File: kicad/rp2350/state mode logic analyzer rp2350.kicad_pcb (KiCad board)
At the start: 4 copper layers, 65.9 x 81.5 mm, 154 parts, among them J1 USB0, J2 5V USB0, J3 Probe_Hi, J4 Probe Power, J5 Probe_Lo, J6 Probe Power, J7 SWD0, SW1 Reset 0, SW2 Boot 0, U12 SN74LVC8T245, U13 SN74LVC2T45DCUR, U2 RP2350_80QFN, U4 SN74LVC8T245, U5 SN74LVC8T245, U6 SN74LVC8T245, U7 IS25LP128F-JBLE, U9 MCP1826S, Y1 ECS-120-18-33-JEM-TR

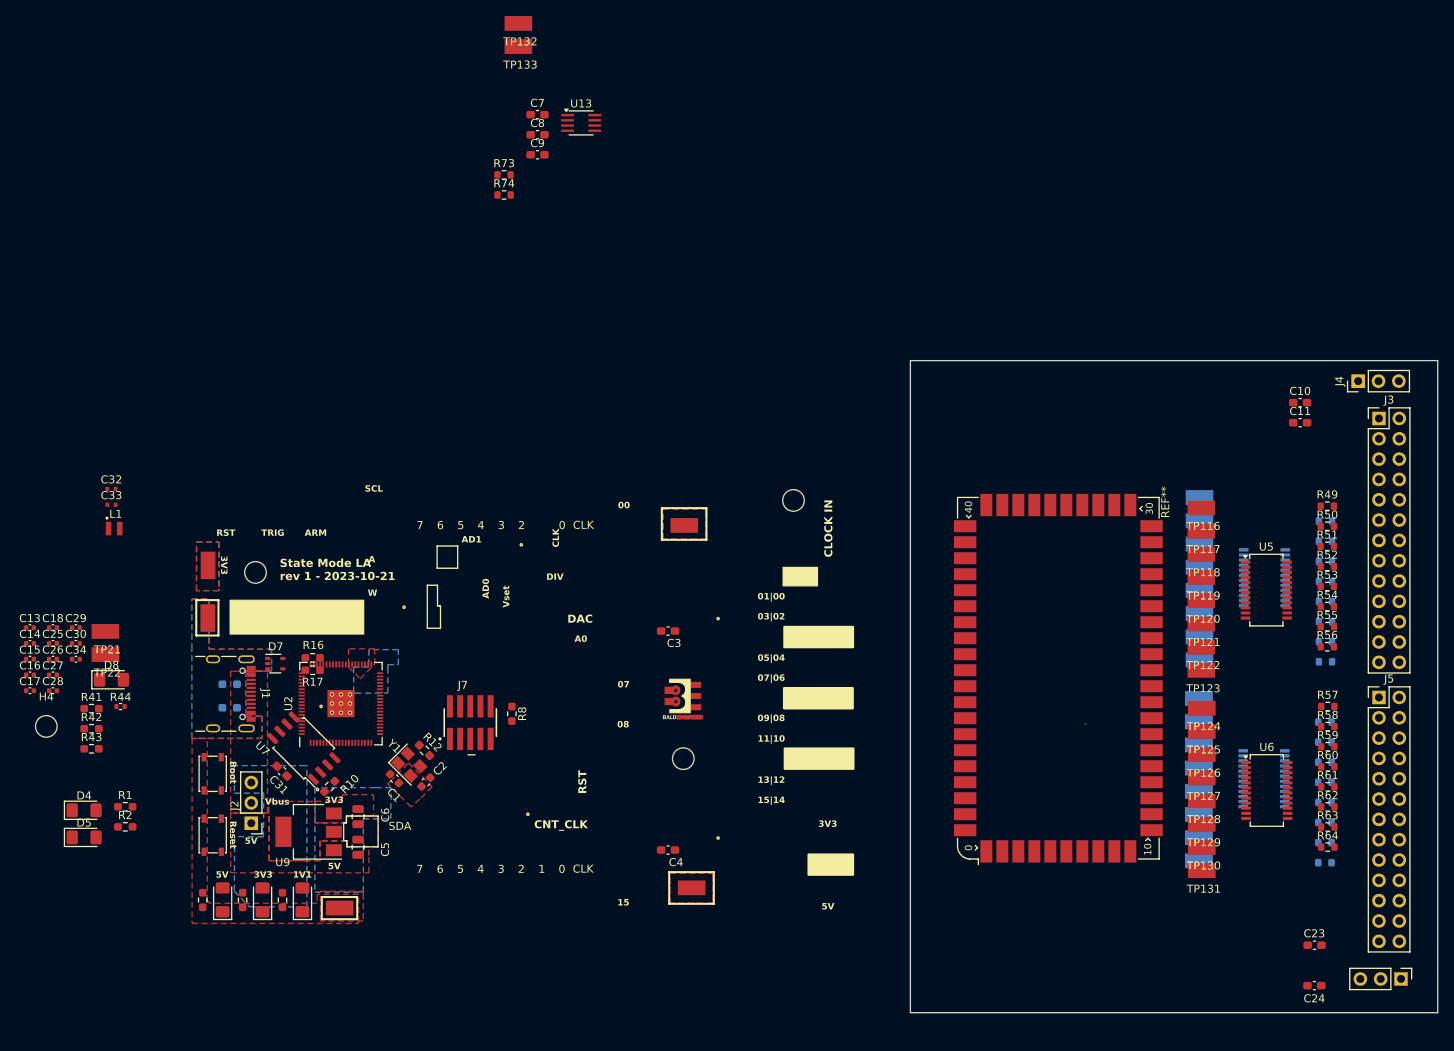
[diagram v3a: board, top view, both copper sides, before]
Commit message: early pcb layout - need to build a demo/test board next
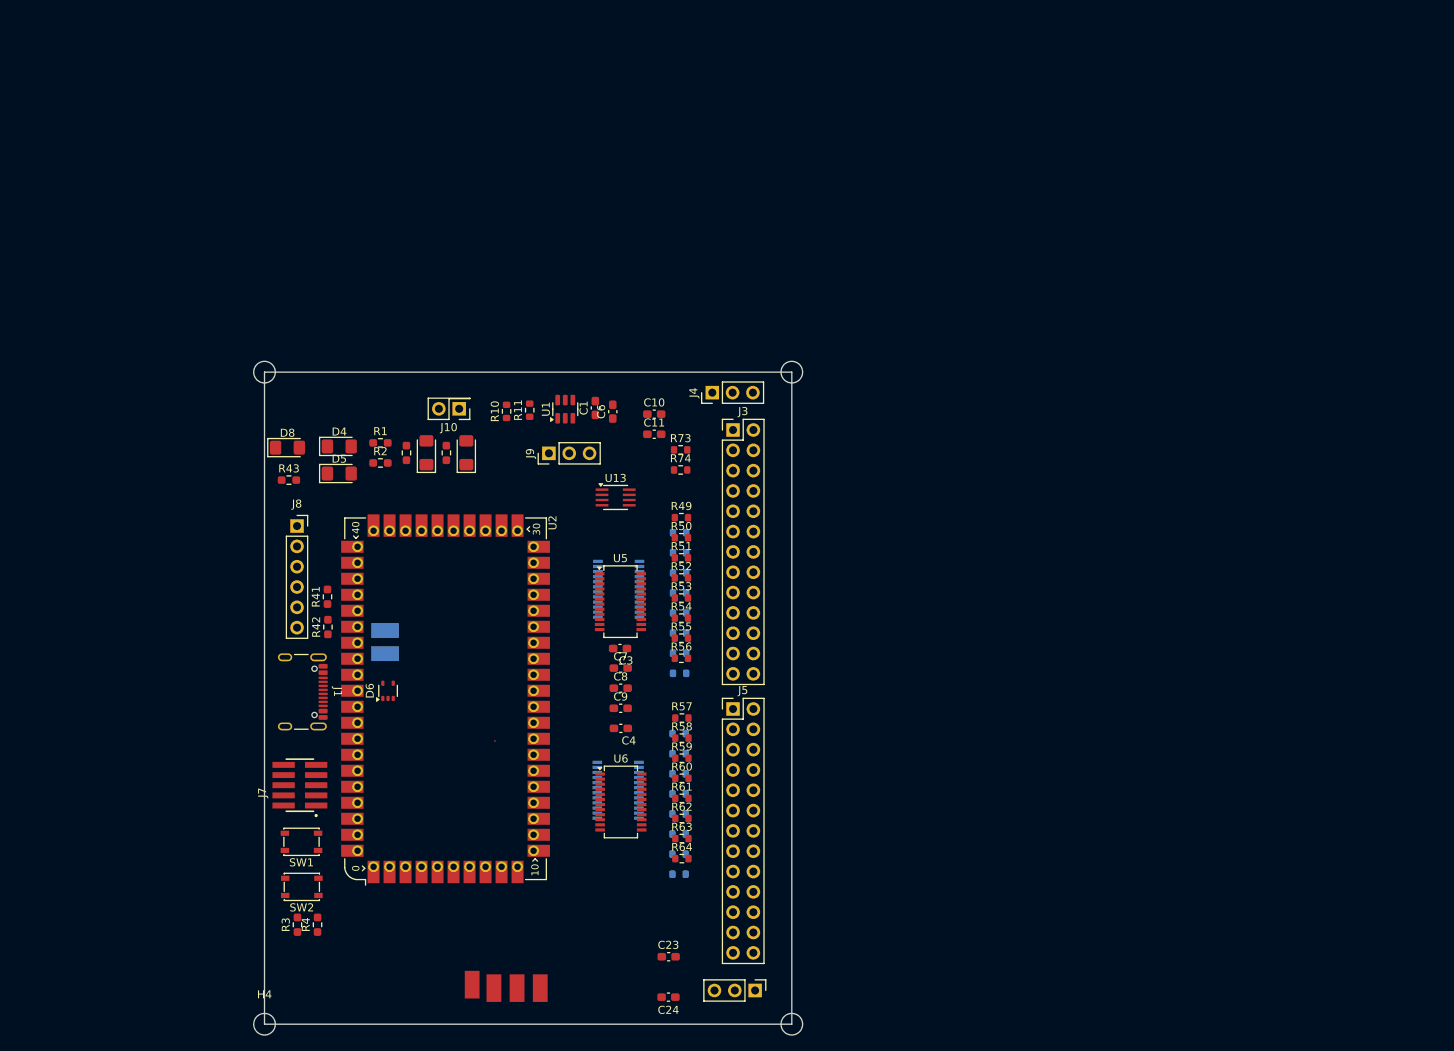
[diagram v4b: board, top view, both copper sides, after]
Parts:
- removed C13, C15, C16, C17, C18, C25, C26, C27, C28, C29, C30: 100n, Capacitor_SMD:C_0402_1005Metric
- removed C14, C34: 4.7u, Capacitor_SMD:C_0402_1005Metric
- removed C2: 27p, Capacitor_SMD:C_0603_1608Metric
- removed C31: 1u, Capacitor_SMD:C_0603_1608Metric_Pad1.08x0.95mm_HandSolder
- removed C32, C33: 4.7u, RP2350_80QFN_minimal:C_0402_1005Metric_small_pads
- removed C5: 10u, Capacitor_SMD:C_0805_2012Metric
- removed D3: 1v1, LED_SMD:LED_1206_3216Metric_Pad1.42x1.75mm_HandSolder
- removed D7: BZA856AVL, Package_TO_SOT_SMD:SOT-353_SC-70-5
- removed J2: 5V USB0, Connector_PinHeader_2.54mm:PinHeader_1x03_P2.54mm_Vertical
- removed L1: 3.3u, RP2350_80QFN_minimal:L_pol_2016
- removed R12: 0, Resistor_SMD:R_0603_1608Metric_Pad0.98x0.95mm_HandSolder
- removed R16, R17: 27, Resistor_SMD:R_0603_1608Metric_Pad0.98x0.95mm_HandSolder
- removed R23, R24: 5k1, Resistor_SMD:R_0603_1608Metric_Pad0.98x0.95mm_HandSolder
- removed R44: 33, Resistor_SMD:R_0402_1005Metric
- removed R7, R8: 4k7, Resistor_SMD:R_0603_1608Metric_Pad0.98x0.95mm_HandSolder
- removed REF**: RP2xxx_Stamp_XL_SMD, KiCad:RP2xxx_Stamp_XL_SMD
- removed REF**: KiCad-Logo_5mm_SilkScreen, Symbol:KiCad-Logo_5mm_SilkScreen
- removed REF**: OSHW-Symbol_8.9x8mm_SilkScreen, Symbol:OSHW-Symbol_8.9x8mm_SilkScreen
- removed TP100, TP101, TP102, TP103, TP104, TP105, TP106, TP107, TP108, TP109, TP110, TP111, TP112, TP113, TP114, TP115, TP116, TP117, TP118, TP119, TP120, TP121, TP122, TP123, TP124, TP125, TP126, TP127, TP128, TP129, TP130, TP131, TP132, TP133, TP15: TestPoint_Harwin, My Libraries:Harwin-S1751-46-Test-Point
- removed U7: IS25LP128F-JBLE, Package_SO:SOIC-8_5.23x5.23mm_P1.27mm
- removed U9: MCP1826S, Package_TO_SOT_SMD:SOT-223
- removed Y1: ECS-120-18-33-JEM-TR, Crystal:Crystal_SMD_3225-4Pin_3.2x2.5mm
- removed svg2mod: G***, My Libraries:BE5v2
- added D6: BZA856AVL, Package_TO_SOT_SMD:SOT-353_SC-70-5, F.Cu at (88.1, 57.8)
- added J10: Vcca_select, Connector_PinHeader_2.54mm:PinHeader_2x01_P2.54mm_Vertical, F.Cu at (97.0, 22.5)
- added J8: FTDI Header, Connector_PinSocket_2.54mm:PinSocket_1x06_P2.54mm_Vertical, F.Cu at (76.7, 37.2)
- added J9: Vccb_select, Connector_PinHeader_2.54mm:PinHeader_1x03_P2.54mm_Vertical, F.Cu at (108.2, 28.1)
- added R11: 1k, Resistor_SMD:R_0603_1608Metric, F.Cu at (105.8, 22.7)
- added R3: 5k1, Resistor_SMD:R_0603_1608Metric_Pad0.98x0.95mm_HandSolder, F.Cu at (76.7, 87.0)
- added R4: 5k1, Resistor_SMD:R_0603_1608Metric_Pad0.98x0.95mm_HandSolder, F.Cu at (79.3, 87.0)
- added U1: MCP4725A2T-E/CH, Package_TO_SOT_SMD:SOT-23-6, F.Cu at (110.2, 22.6)
- C1: value 27p -> 100n; footprint Capacitor_SMD:C_0603_1608Metric -> Capacitor_SMD:C_0603_1608Metric_Pad1.08x0.95mm_HandSolder
- C6: footprint Capacitor_SMD:C_0805_2012Metric -> Capacitor_SMD:C_0603_1608Metric_Pad1.08x0.95mm_HandSolder
- D8: value 2040_L0 -> 2350_LED
- R10: value 1k -> 0; footprint Resistor_SMD:R_0603_1608Metric_Pad0.98x0.95mm_HandSolder -> Resistor_SMD:R_0603_1608Metric
- SW1: value Reset 0 -> Reset
- SW2: value Boot 0 -> Boot
- TP21, TP22: moved to B.Cu
- U2: value RP2350_80QFN -> RP2350_Stamp_XL; footprint RP2350_80QFN_minimal:RP2350-QFN-80-1EP_10x10_P0.4mm_EP3.4x3.4mm_ThermalVias -> RP2xxx_Stamp:RP2xxx_Stamp_XL_THT
- moved C24 80.8 mm to (123.1, 96.1)
- moved U12 80.8 mm to (116.8, 70.2)
- moved U4 80.8 mm to (116.9, 45.1)
- moved U5 80.8 mm to (117.1, 46.6)
- moved C10 80.8 mm to (121.3, 23.2)
- moved C11 80.8 mm to (121.3, 25.7)
- moved J3 80.8 mm to (131.2, 25.2)
- moved J4 80.8 mm to (128.6, 20.5)
- moved J5 80.8 mm to (131.2, 60.0)
- moved J6 80.8 mm to (134.0, 95.2)
- moved R57 80.8 mm to (124.8, 61.2)
- moved R58 80.8 mm to (124.8, 63.7)
- moved R59 80.8 mm to (124.8, 66.2)
- moved R60 80.8 mm to (124.8, 68.7)
- moved R61 80.8 mm to (124.8, 71.2)
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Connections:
- C1 pad 1: Net-(U2-XIN) -> Net-(J9-Pin_3)
- C6 pad 1: +3V3 -> +5V
- J1 pad A4: /VBUS -> +5V
- J1 pad A6: /USB_DP -> /DP
- J1 pad A7: /USB_DN -> /DN
- J1 pad A9: /VBUS -> +5V
- J1 pad B4: /VBUS -> +5V
- J1 pad B6: /USB_DP -> /DP
- J1 pad B7: /USB_DN -> /DN
- J1 pad B9: /VBUS -> +5V
- J7 pad 10: /Run -> /Reset
- R1 pad 1: Net-(U2-GPIO47_ADC7) -> /Armed
- R10 pad 1: /~{CS} -> Net-(U1-VOUT)
- R10 pad 2: Net-(R10-Pad2) -> Net-(J9-Pin_3)
- R2 pad 1: Net-(U2-GPIO46_ADC6) -> /Triggered
- R41 pad 2: /SDA -> /I2C1_SDA
- R42 pad 2: /SCL -> /I2C1_SCL
- R43 pad 1: /CNT_RESET -> /2350_LED
- SW1 pad 1: /Run -> /Reset
- SW2 pad 1: Net-(R10-Pad2) -> Net-(U2A-BOOTSEL)
- TP21 pad 1: /SDA -> /I2C1_SDA
- TP22 pad 1: /SCL -> /I2C1_SCL
- U12 pad 1: +3V3 -> Vcca
- U12 pad 2: unconnected-(U12-DIR-Pad2) -> GND
- U12 pad 22: unconnected-(U12-~{OE}-Pad22) -> GND
- U12 pad 23: +3V3 -> Vccb
- U12 pad 24: +3V3 -> Vccb
- U13 pad 1: +3V3 -> Vcca
- U13 pad 5: unconnected-(U13-DIR-Pad5) -> GND
- U13 pad 8: +3V3 -> Vccb
- U2 pad 1: /BUF29 -> /QUAL
- U2 pad 10: +1V1 -> /BUF24
- U2 pad 11: /BUF21 -> /BUF23
- U2 pad 12: /BUF20 -> /BUF22
- U2 pad 13: /BUF19 -> /BUF21
- U2 pad 14: /BUF18 -> /BUF20
- U2 pad 15: +3V3 -> /BUF19
- U2 pad 16: /BUF17 -> /BUF18
- U2 pad 17: /BUF16 -> /BUF17
- U2 pad 18: /QUAL -> /BUF16
- U2 pad 19: /CLK -> /QUAL
- U2 pad 2: /BUF28 -> /CLK
- U2 pad 20: /BUF15 -> /CLK
- U2 pad 21: /BUF14 -> /BUF15
- U2 pad 22: /BUF13 -> /BUF14
- U2 pad 23: /BUF12 -> /BUF13
- U2 pad 24: +3V3 -> /BUF12
- U2 pad 29: +3V3 -> /BUF07
- U2 pad 3: /BUF27 -> /BUF31
- U2 pad 30: Net-(U2-XIN) -> /BUF06
- U2 pad 31: Net-(U2-XOUT) -> GND
- U2 pad 32: +1V1 -> unconnected-(U2A-VBAT-Pad32)_1
- U2 pad 33: /SWCLK -> +5V
- U2 pad 34: /SWD -> +3V3
- U2 pad 35: /Run -> /DN
- U2 pad 36: /BUF07 -> /DP
- U2 pad 37: /BUF06 -> /SWD
- U2 pad 38: /BUF05 -> /SWCLK
- U2 pad 39: /BUF04 -> /Reset
- U2 pad 4: /BUF26 -> /BUF30
- U2 pad 40: /BUF03 -> Net-(U2A-BOOTSEL)
- U2 pad 41: +3V3 -> /BUF05
- U2 pad 42: /BUF02 -> /BUF04
- U2 pad 43: /BUF01 -> /BUF03
- U2 pad 44: /BUF00 -> /BUF02
- U2 pad 45: unconnected-(U2-GPIO36-Pad45) -> /BUF01
- U2 pad 46: unconnected-(U2-GPIO37-Pad46) -> /BUF00
- U2 pad 5: +3V3 -> /BUF29
- U2 pad 50: +3V3 -> unconnected-(U2B-GPIO39-Pad50)
- U2 pad 51: +1V1 -> /Armed
- U2 pad 52: /SDA -> /Triggered
- U2 pad 53: /SCL -> /2350_LED
- U2 pad 54: /CNT_CLK -> unconnected-(U2B-GPIO43-Pad54)_1
- U2 pad 55: /CNT_RESET -> /UART_TX
- U2 pad 56: /LA_Enable -> /UART_RX
- U2 pad 57: Net-(U2-GPIO46_ADC6) -> /I2C1_SDA
- U2 pad 58: Net-(U2-GPIO47_ADC7) -> /I2C1_SCL
- U2 pad 59: +3V3 -> unconnected-(U2A-BAT_STAT-Pad59)
- U2 pad 6: /BUF25 -> /BUF28
- U2 pad 60: +3V3 -> unconnected-(U2A-LDO_EN-Pad60)
- U2 pad 7: /BUF24 -> /BUF27
- U2 pad 8: /BUF23 -> /BUF26
- U2 pad 9: /BUF22 -> /BUF25
- U4 pad 1: +3V3 -> Vcca
- U4 pad 2: unconnected-(U4-DIR-Pad2) -> GND
- U4 pad 22: unconnected-(U4-~{OE}-Pad22) -> GND
- U4 pad 23: +3V3 -> Vccb
- U4 pad 24: +3V3 -> Vccb
- U5 pad 1: +3V3 -> Vcca
- U5 pad 2: unconnected-(U5-DIR-Pad2) -> GND
- U5 pad 22: unconnected-(U5-~{OE}-Pad22) -> GND
- U5 pad 23: +3V3 -> Vccb
- U5 pad 24: +3V3 -> Vccb
- U6 pad 1: +3V3 -> Vcca
- U6 pad 2: unconnected-(U6-DIR-Pad2) -> GND
- U6 pad 22: unconnected-(U6-~{OE}-Pad22) -> GND
- U6 pad 23: +3V3 -> Vccb
- U6 pad 24: +3V3 -> Vccb
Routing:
- removed copper zone on B.Cu, net +3V3
- removed copper zone on F.Cu, net +3V3
- removed copper zone on In2.Cu, net +3V3
- removed copper zone on F.Cu, net +5V
- removed copper zone on F.Cu, net /VBUS
- removed copper zone on B.Cu, net GND
- removed copper zone on F.Cu, net GND
- removed copper zone on In1.Cu, net GND
- removed copper zone on In2.Cu, net GND
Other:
- board text added: "Verify courtyard of FISH"
- board text removed: "0"
- board text removed: "00"
- board text removed: "01|00"
- board text removed: "03|02"
- board text removed: "05|04"
- board text removed: "07"
- board text removed: "07|06"
- board text removed: "08"
- board text removed: "09|08"
- board text removed: "1"
- board text removed: "11|10"
- board text removed: "13|12"
- board text removed: "15"
- board text removed: "15|14"
- board text removed: "1V1"
- board text removed: "2"
- board text removed: "3"
- board text removed: "3V3"
- board text removed: "4"
- board text removed: "5"
- board text removed: "5V"
- board text removed: "6"
- board text removed: "7"
- board text removed: "A"
- board text removed: "A0"
- board text removed: "AD0"
- board text removed: "AD1"
- board text removed: "ARM"
- board text removed: "Boot"
- board text removed: "CLK"
- board text removed: "CLOCK IN"
- board text removed: "CNT_CLK"
- board text removed: "DAC"
- board text removed: "DIV"
- board text removed: "RST"
- board text removed: "Reset"
- board text removed: "SCL"
- board text removed: "SDA"
- board text removed: "State Mode LA rev 1 - 2023-10-21"
- board text removed: "TRIG"
- board text removed: "Vbus"
- board text removed: "Vset"
- board text removed: "W"

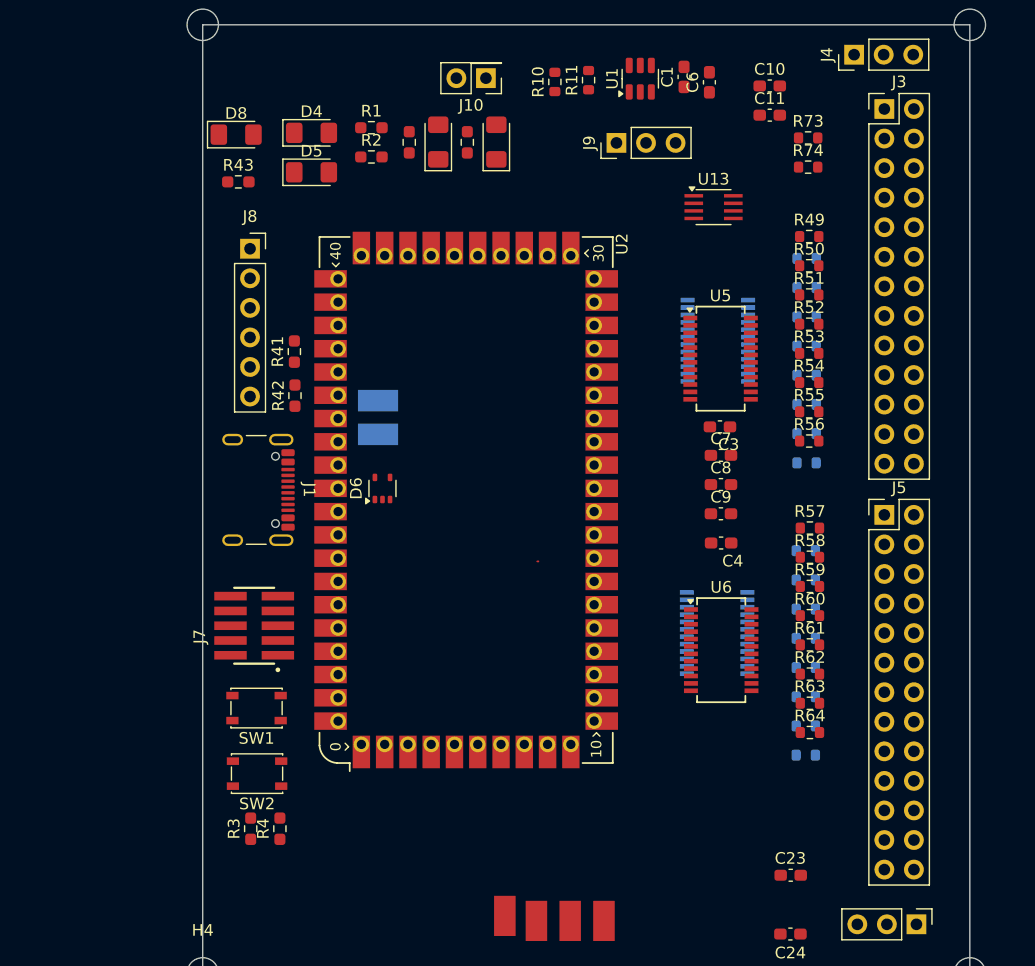
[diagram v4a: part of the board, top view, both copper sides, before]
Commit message: updated buffer PNs and reordered pins to match XL pinout
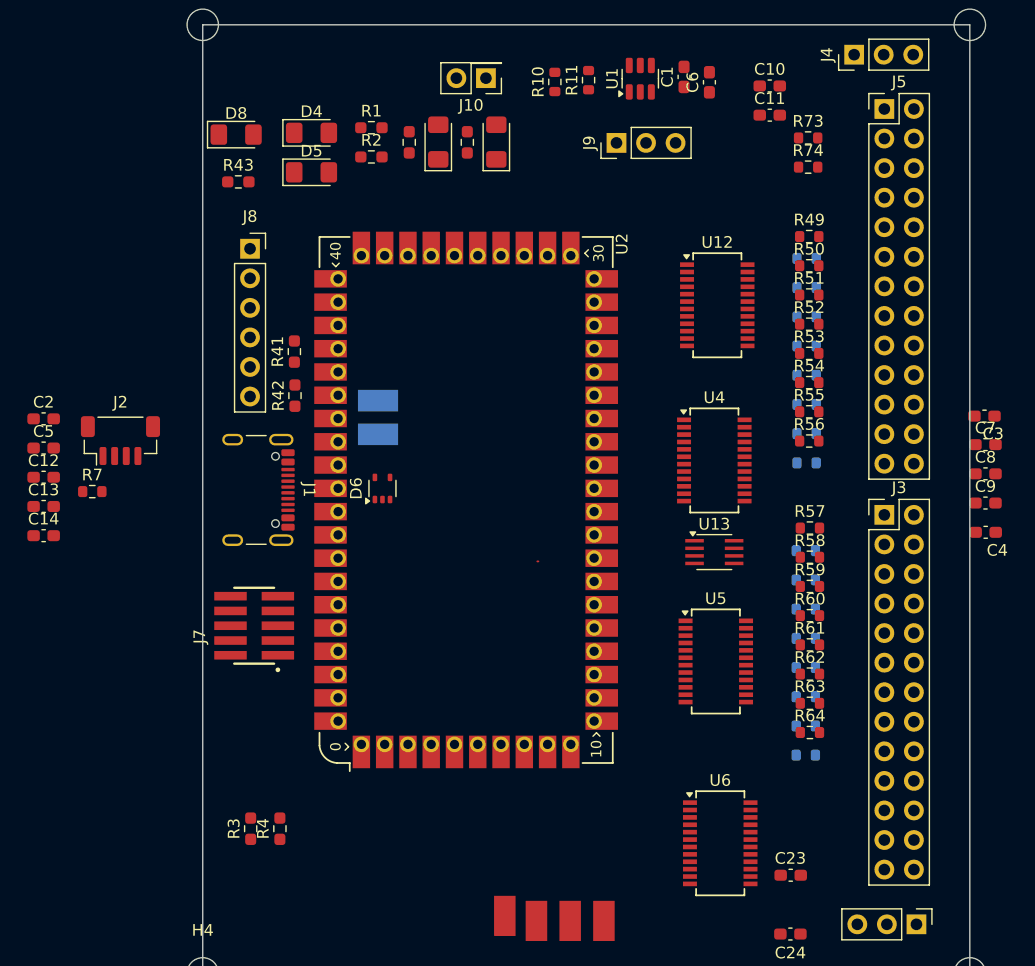
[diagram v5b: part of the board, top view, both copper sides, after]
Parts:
- removed SW1: Reset, Button_Switch_SMD:SW_SPST_PTS810
- removed SW2: Boot, Button_Switch_SMD:SW_SPST_PTS810
- added C12: 1u, Capacitor_SMD:C_0603_1608Metric_Pad1.08x0.95mm_HandSolder, F.Cu at (59.0, 56.8)
- added C13: 1u, Capacitor_SMD:C_0603_1608Metric_Pad1.08x0.95mm_HandSolder, F.Cu at (59.0, 59.3)
- added C14: 1u, Capacitor_SMD:C_0603_1608Metric_Pad1.08x0.95mm_HandSolder, F.Cu at (59.0, 61.8)
- added C2: 1u, Capacitor_SMD:C_0603_1608Metric_Pad1.08x0.95mm_HandSolder, F.Cu at (59.0, 51.8)
- added C5: 1u, Capacitor_SMD:C_0603_1608Metric_Pad1.08x0.95mm_HandSolder, F.Cu at (59.0, 54.3)
- added J2: JST_SH_BM04B-SRSS-TB, Connector_JST:JST_SH_BM04B-SRSS-TB_1x04-1MP_P1.00mm_Vertical, F.Cu at (65.6, 53.7)
- added R7: 10k, Resistor_SMD:R_0603_1608Metric, F.Cu at (63.1, 58.0)
- R11: value 1k -> 10k
- U12, U4: value SN74LVC8T245 -> SN74LVC8T245DBQR; moved to F.Cu
- U13: value SN74LVC2T45DCUR -> SN74LVC2T45DCTRE4
- U5, U6: value SN74LVC8T245 -> SN74LVC8T245DBQR
- moved J3 34.9 mm to (131.2, 60.0)
- moved J5 34.9 mm to (131.2, 25.2)
- moved U13 29.6 mm to (116.6, 63.2)
- moved U12 28.2 mm to (116.8, 42.0)
- moved U5 26.0 mm to (116.7, 72.6)
- moved C3 22.8 mm to (139.8, 51.6)
- moved C4 22.8 mm to (139.9, 61.5)
- moved C7 22.8 mm to (139.9, 54.0)
- moved C8 22.8 mm to (139.9, 56.5)
- moved C9 22.8 mm to (139.9, 59.0)
- moved U6 16.6 mm to (117.1, 88.3)
- moved U4 10.3 mm to (116.6, 55.4)
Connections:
- C3 pad 1: +3V3 -> Vccb
- C4 pad 1: +3V3 -> Vccb
- C7 pad 1: +3V3 -> Vccb
- C8 pad 1: +3V3 -> Vccb
- C9 pad 1: +3V3 -> Vccb
- R11 pad 1: GND -> /Vdac
- R25 pad 2: /IN00 -> /IN07
- R26 pad 2: /IN01 -> /IN06
- R27 pad 2: /IN02 -> /IN05
- R28 pad 2: /IN03 -> /IN04
- R29 pad 2: /IN04 -> /IN03
- R30 pad 2: /IN05 -> /IN02
- R31 pad 2: /IN06 -> /IN01
- R32 pad 2: /IN07 -> /IN00
- R33 pad 2: /IN15 -> /IN08
- R34 pad 2: /IN14 -> /IN09
- R35 pad 2: /IN13 -> /IN10
- R36 pad 2: /IN12 -> /IN11
- R37 pad 2: /IN11 -> /IN12
- R38 pad 2: /IN10 -> /IN13
- R39 pad 2: /IN09 -> /IN14
- R40 pad 2: /IN08 -> /IN15
- R49 pad 2: /IN23 -> /IN16
- R50 pad 2: /IN22 -> /IN17
- R51 pad 2: /IN21 -> /IN18
- R52 pad 2: /IN20 -> /IN19
- R53 pad 2: /IN19 -> /IN20
- R54 pad 2: /IN18 -> /IN21
- R55 pad 2: /IN17 -> /IN22
- R56 pad 2: /IN16 -> /IN23
- R57 pad 2: /IN31 -> /IN24
- R58 pad 2: /IN30 -> /IN25
- R59 pad 2: /IN29 -> /IN26
- R60 pad 2: /IN28 -> /IN27
- R61 pad 2: /IN27 -> /IN28
- R62 pad 2: /IN26 -> /IN29
- R63 pad 2: /IN25 -> /IN30
- R64 pad 2: /IN24 -> /IN31
- U12 pad 10: /BUF00 -> /BUF07
- U12 pad 3: /BUF07 -> /BUF00
- U12 pad 4: /BUF06 -> /BUF01
- U12 pad 5: /BUF05 -> /BUF02
- U12 pad 6: /BUF04 -> /BUF03
- U12 pad 7: /BUF03 -> /BUF04
- U12 pad 8: /BUF02 -> /BUF05
- U12 pad 9: /BUF01 -> /BUF06
- U2 pad 39: /Reset -> unconnected-(U2A-~{RESET}-Pad39)
- U2 pad 40: Net-(U2A-BOOTSEL) -> unconnected-(U2A-BOOTSEL-Pad40)_1
- U2 pad 54: unconnected-(U2B-GPIO43-Pad54)_1 -> /Vdac
- U4 pad 10: /BUF08 -> /BUF15
- U4 pad 3: /BUF15 -> /BUF08
- U4 pad 4: /BUF14 -> /BUF09
- U4 pad 5: /BUF13 -> /BUF10
- U4 pad 6: /BUF12 -> /BUF11
- U4 pad 7: /BUF11 -> /BUF12
- U4 pad 8: /BUF10 -> /BUF13
- U4 pad 9: /BUF09 -> /BUF14
- U5 pad 10: /BUF16 -> /BUF23
- U5 pad 3: /BUF23 -> /BUF16
- U5 pad 4: /BUF22 -> /BUF17
- U5 pad 5: /BUF21 -> /BUF18
- U5 pad 6: /BUF20 -> /BUF19
- U5 pad 7: /BUF19 -> /BUF20
- U5 pad 8: /BUF18 -> /BUF21
- U5 pad 9: /BUF17 -> /BUF22
- U6 pad 10: /BUF24 -> /BUF31
- U6 pad 3: /BUF31 -> /BUF24
- U6 pad 4: /BUF30 -> /BUF25
- U6 pad 5: /BUF29 -> /BUF26
- U6 pad 6: /BUF28 -> /BUF27
- U6 pad 7: /BUF27 -> /BUF28
- U6 pad 8: /BUF26 -> /BUF29
- U6 pad 9: /BUF25 -> /BUF30
